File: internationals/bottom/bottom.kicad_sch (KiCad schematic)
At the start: 25 parts, among them U3 ESP-S2-Pico

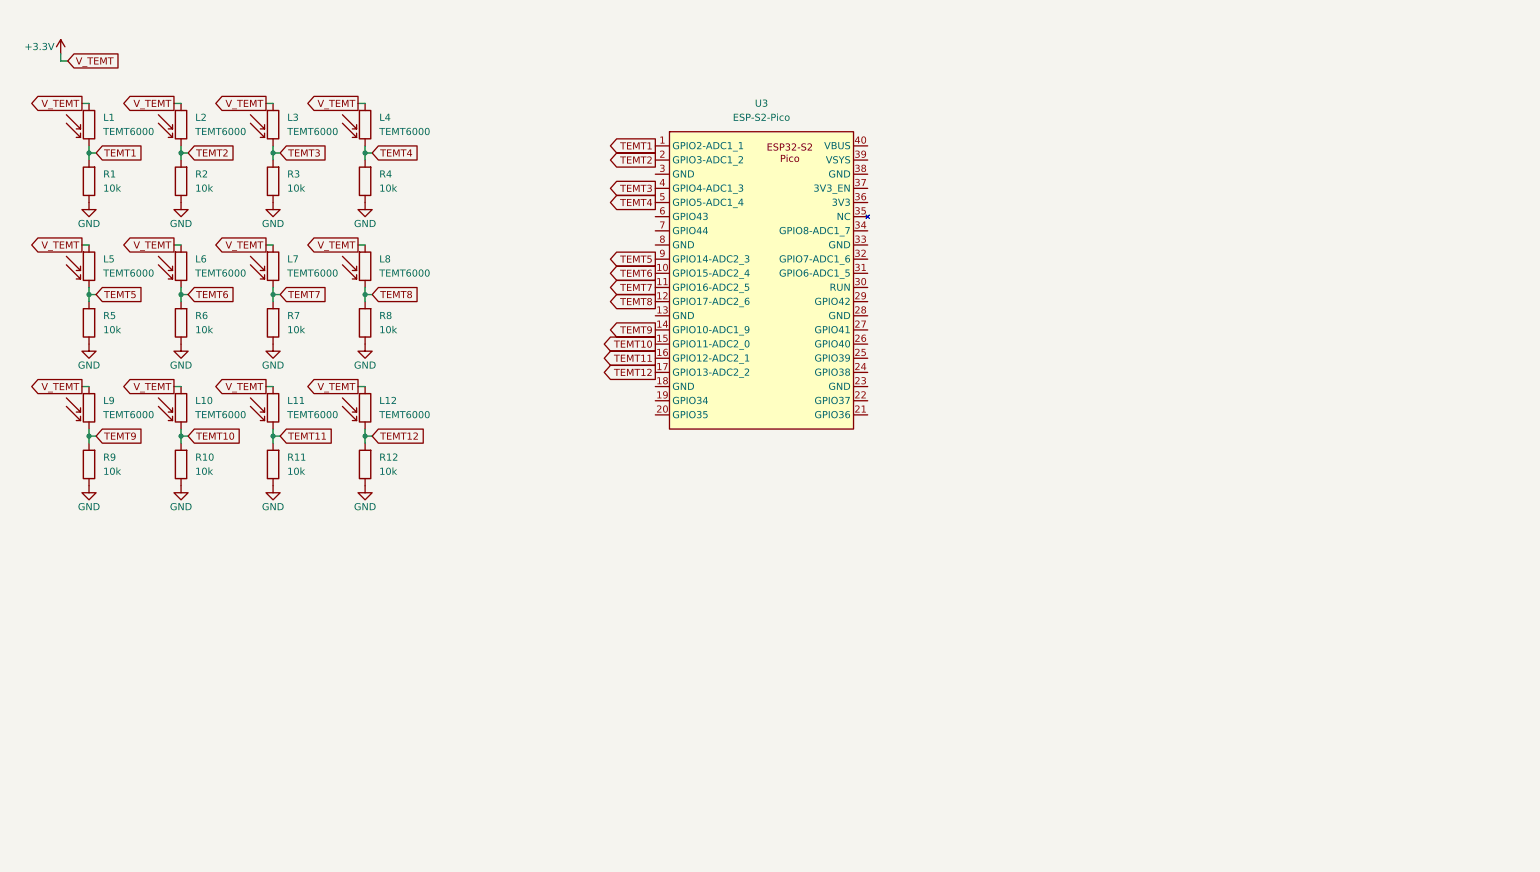
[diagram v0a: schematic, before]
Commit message: pcbs: feat: update and complete bottom plate schematics
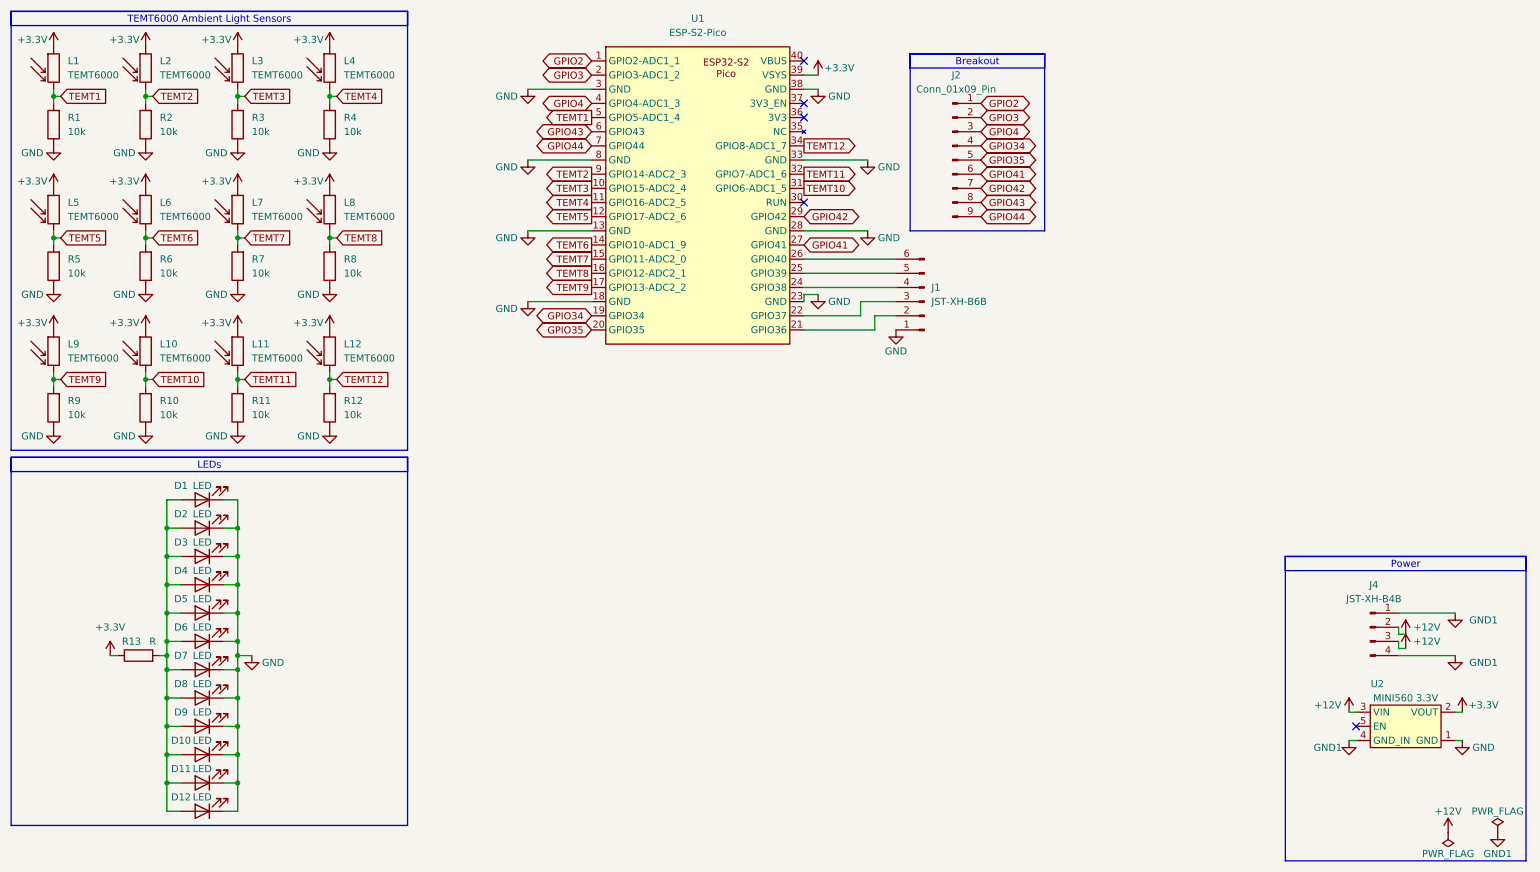
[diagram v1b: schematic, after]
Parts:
- added D1, D10, D11, D12, D2, D3, D4, D5, D6, D7, D8, D9: LED, PorridgePi-Personal:LED-6028-SMD, symbol Device:LED
- added J1: JST-XH-B6B, Connector_JST:JST_XH_B6B-XH-A_1x06_P2.50mm_Vertical, symbol Connector:Conn_01x06_Pin
- added J2: Conn_01x09_Pin, Connector_PinHeader_2.54mm:PinHeader_1x09_P2.54mm_Vertical, symbol Connector:Conn_01x09_Pin
- added J4: JST-XH-B4B, Connector_JST:JST_XH_B4B-XH-A_1x04_P2.50mm_Vertical, symbol Connector:Conn_01x04_Pin
- added R13: R, PCM_Resistor_THT_AKL:R_Axial_DIN0204_L3.6mm_D1.6mm_P5.08mm_Horizontal, symbol Device:R
- added U2: MINI560 3.3V, PorridgePi-Personal:MINI560, symbol PorridgePi-Symbols:VREG-Voltage-Regulator
- renumbered U3 to U1
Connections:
- net +3.3V: now also U1.39 (VSYS), R13.1, U2.2 (VOUT)
- net GND: now also U1.13 (GND), U1.18 (GND), U1.23 (GND), U1.28 (GND), U1.3 (GND), U1.33 (GND), U1.38 (GND), U1.8 (GND), D1.1 (K), D10.1 (K), D11.1 (K), D12.1 (K), D2.1 (K), D3.1 (K), D4.1 (K), D5.1 (K), D6.1 (K), D7.1 (K), D8.1 (K), D9.1 (K), J1.1 (Pin_1), U2.1 (GND)
- net TEMT1: now also U1.5 (GPIO5-ADC1_4); no longer U1.1 (GPIO2-ADC1_1)
- net TEMT10: now also U1.31 (GPIO6-ADC1_5); no longer U1.15 (GPIO11-ADC2_0)
- net TEMT11: now also U1.32 (GPIO7-ADC1_6); no longer U1.16 (GPIO12-ADC2_1)
- net TEMT12: now also U1.34 (GPIO8-ADC1_7); no longer U1.17 (GPIO13-ADC2_2)
- net TEMT2: now also U1.9 (GPIO14-ADC2_3); no longer U1.2 (GPIO3-ADC1_2)
- net TEMT3: now also U1.10 (GPIO15-ADC2_4); no longer U1.4 (GPIO4-ADC1_3)
- net TEMT4: now also U1.11 (GPIO16-ADC2_5); no longer U1.5 (GPIO5-ADC1_4)
- net TEMT5: now also U1.12 (GPIO17-ADC2_6); no longer U1.9 (GPIO14-ADC2_3)
- net TEMT6: now also U1.14 (GPIO10-ADC1_9); no longer U1.10 (GPIO15-ADC2_4)
- net TEMT7: now also U1.15 (GPIO11-ADC2_0); no longer U1.11 (GPIO16-ADC2_5)
- net TEMT8: now also U1.16 (GPIO12-ADC2_1); no longer U1.12 (GPIO17-ADC2_6)
- net TEMT9: now also U1.17 (GPIO13-ADC2_2); no longer U1.14 (GPIO10-ADC1_9)
- net GPIO34: now reaches U1.19 (GPIO34)
- net GPIO34: now also J2.4 (Pin_4)
- net GPIO35: now reaches U1.20 (GPIO35)
- net GPIO35: now also J2.5 (Pin_5)
- net at U1.21 (GPIO36): now also J1.2 (Pin_2)
- net at U1.22 (GPIO37): now also J1.3 (Pin_3)
- net at U1.24 (GPIO38): now also J1.4 (Pin_4)
- net at U1.25 (GPIO39): now also J1.5 (Pin_5)
- net at U1.26 (GPIO40): now also J1.6 (Pin_6)
- net GPIO41: now reaches U1.27 (GPIO41)
- net GPIO41: now also J2.6 (Pin_6)
- net GPIO42: now reaches U1.29 (GPIO42)
- net GPIO42: now also J2.7 (Pin_7)
- net GPIO43: now reaches U1.6 (GPIO43)
- net GPIO43: now also J2.8 (Pin_8)
- net GPIO44: now reaches U1.7 (GPIO44)
- net GPIO44: now also J2.9 (Pin_9)
- new net: D1.2 (A), D10.2 (A), D11.2 (A), D12.2 (A), D2.2 (A), D3.2 (A), D4.2 (A), D5.2 (A), D6.2 (A), D7.2 (A), D8.2 (A), D9.2 (A), R13.2
- new net +12V: J4.2 (Pin_2), J4.3 (Pin_3), U2.3 (VIN)
- new net GND1: J4.1 (Pin_1), J4.4 (Pin_4), U2.4 (GND_IN)
- new net GPIO2: J2.1 (Pin_1), U1.1 (GPIO2-ADC1_1)
- new net GPIO3: J2.2 (Pin_2), U1.2 (GPIO3-ADC1_2)
- new net GPIO4: J2.3 (Pin_3), U1.4 (GPIO4-ADC1_3)
- no-connect marks 0 -> 5
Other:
- company: (none) -> Zhou Yikun & Zachary Ang
- title: (none) -> Bottom Plate
- moved on the sheet: L1, R1, U1

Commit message: pcbs: bottom: fix: incorrect label directions and use UART pins
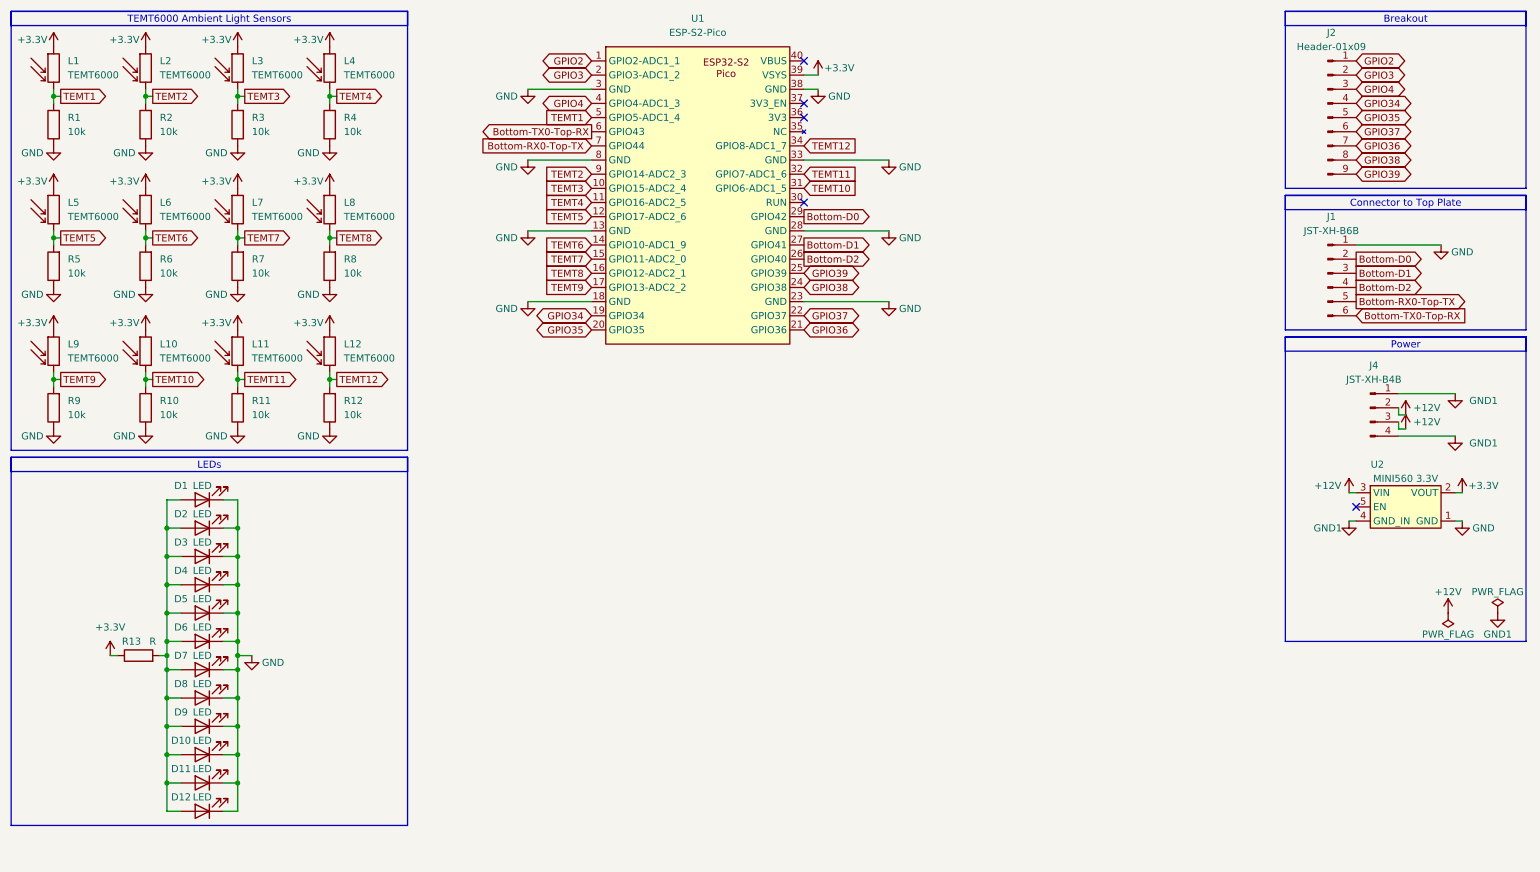
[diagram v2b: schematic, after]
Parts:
- J2: value Conn_01x09_Pin -> Header-01x09
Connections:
- net Bottom-D0: now reaches J1.2 (Pin_2)
- net Bottom-D0: now also U1.29 (GPIO42); no longer U1.21 (GPIO36)
- net Bottom-D1: now reaches J1.3 (Pin_3)
- net Bottom-D1: now also U1.27 (GPIO41); no longer U1.22 (GPIO37)
- net Bottom-D2: now reaches J1.4 (Pin_4)
- net Bottom-D2: now also U1.26 (GPIO40); no longer U1.24 (GPIO38)
- net Bottom-RX0-Top-TX: now reaches J1.5 (Pin_5)
- net Bottom-RX0-Top-TX: now also U1.7 (GPIO44); no longer U1.25 (GPIO39)
- net Bottom-TX0-Top-RX: now reaches J1.6 (Pin_6)
- net Bottom-TX0-Top-RX: now also U1.6 (GPIO43); no longer U1.26 (GPIO40)
- net GPIO41 renamed GPIO37
- net GPIO37: now also U1.22 (GPIO37); no longer U1.27 (GPIO41)
- net GPIO42 renamed GPIO36
- net GPIO36: now also U1.21 (GPIO36); no longer U1.29 (GPIO42)
- net GPIO43 renamed GPIO38
- net GPIO38: now also U1.24 (GPIO38); no longer U1.6 (GPIO43)
- net GPIO44 renamed GPIO39
- net GPIO39: now also U1.25 (GPIO39); no longer U1.7 (GPIO44)
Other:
- moved on the sheet: J2, J4, U2
